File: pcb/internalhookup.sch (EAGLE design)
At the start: 10 parts, among them CN1 LASER, J1 CONTROL, J2 SERVO, J3 AZ_SENSOR, Q1 SMMBT2222ALT, Q2 SMMBT2222ALT, U1 AMS1117-3.3

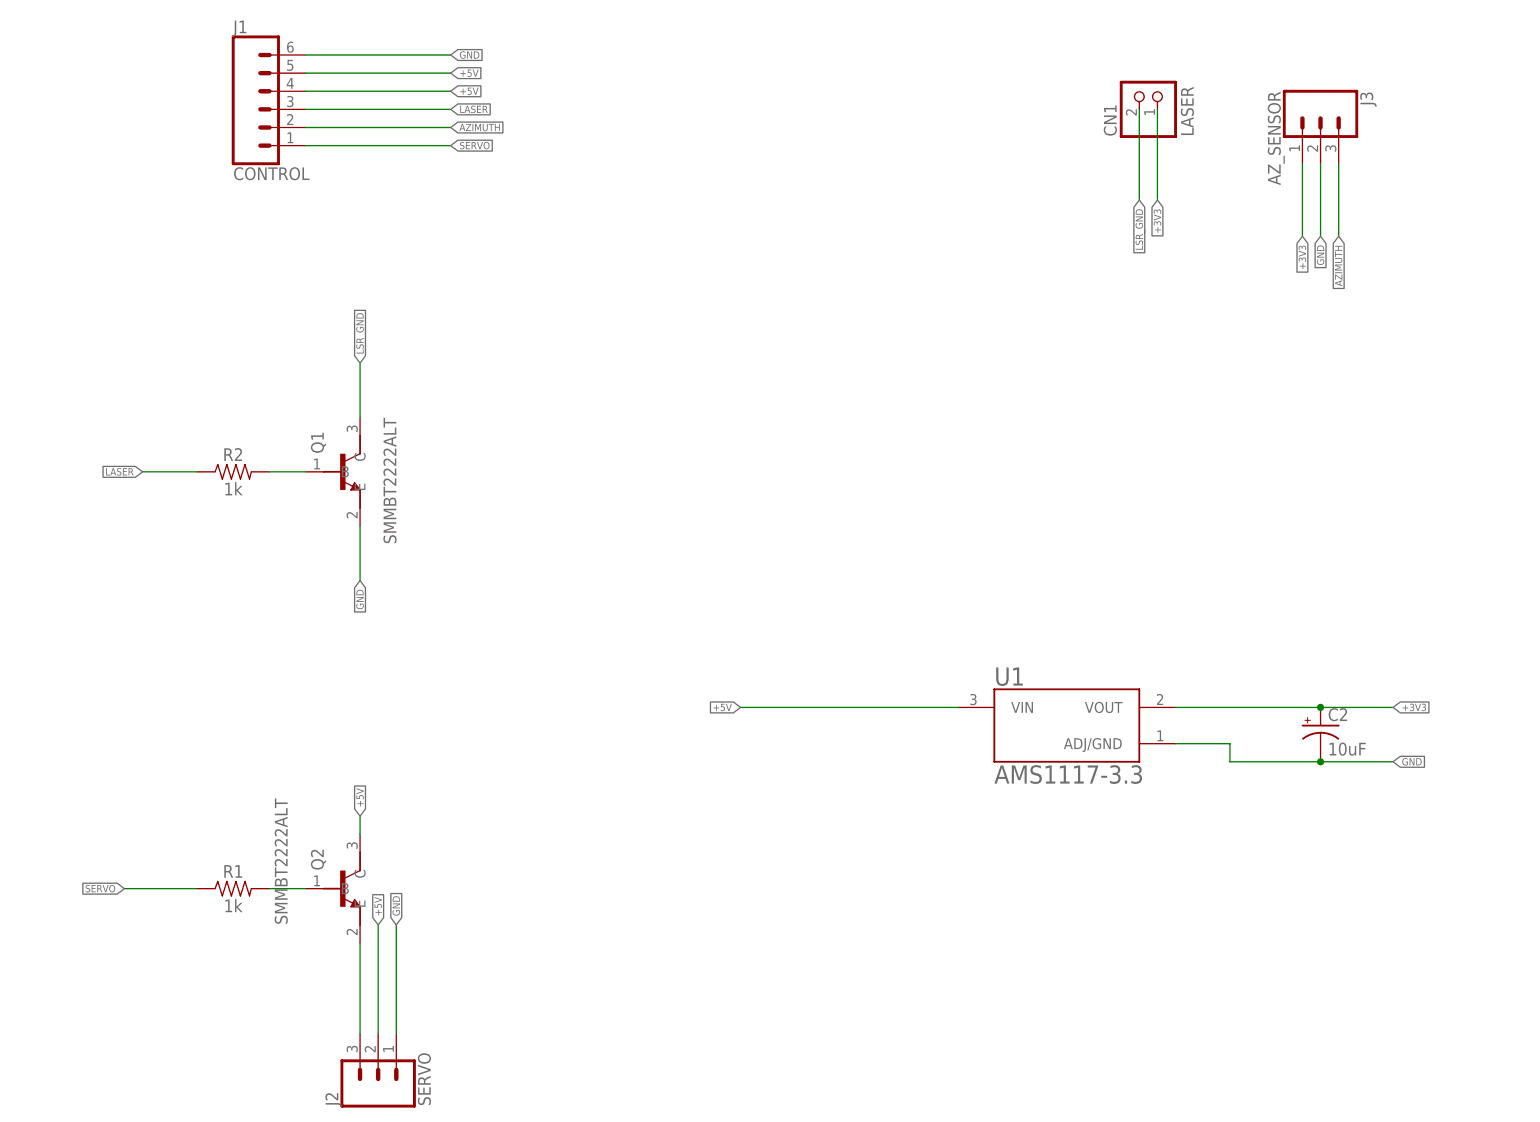
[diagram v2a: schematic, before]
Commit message: Lots of changes
* Dropped LED's and LASER control
* Renamed DECLINATION to AZIMUTH
* Moved AZIMUTH control hookup into the globe (it needs to spin freely)

I couldn't make the LED's fit and shine without casting shadows inside
the globe. Plus, there wasn't much room, and it required more wires to
make work. No a critical problem, but the challenges outweighed the
benefits. I'm going to water color paint the globe now.

I also removed the LASER control, the manufacturer said don't duty cycle
it, the built in controls take care of it. This isn't supposed to be on
constantly anyway.
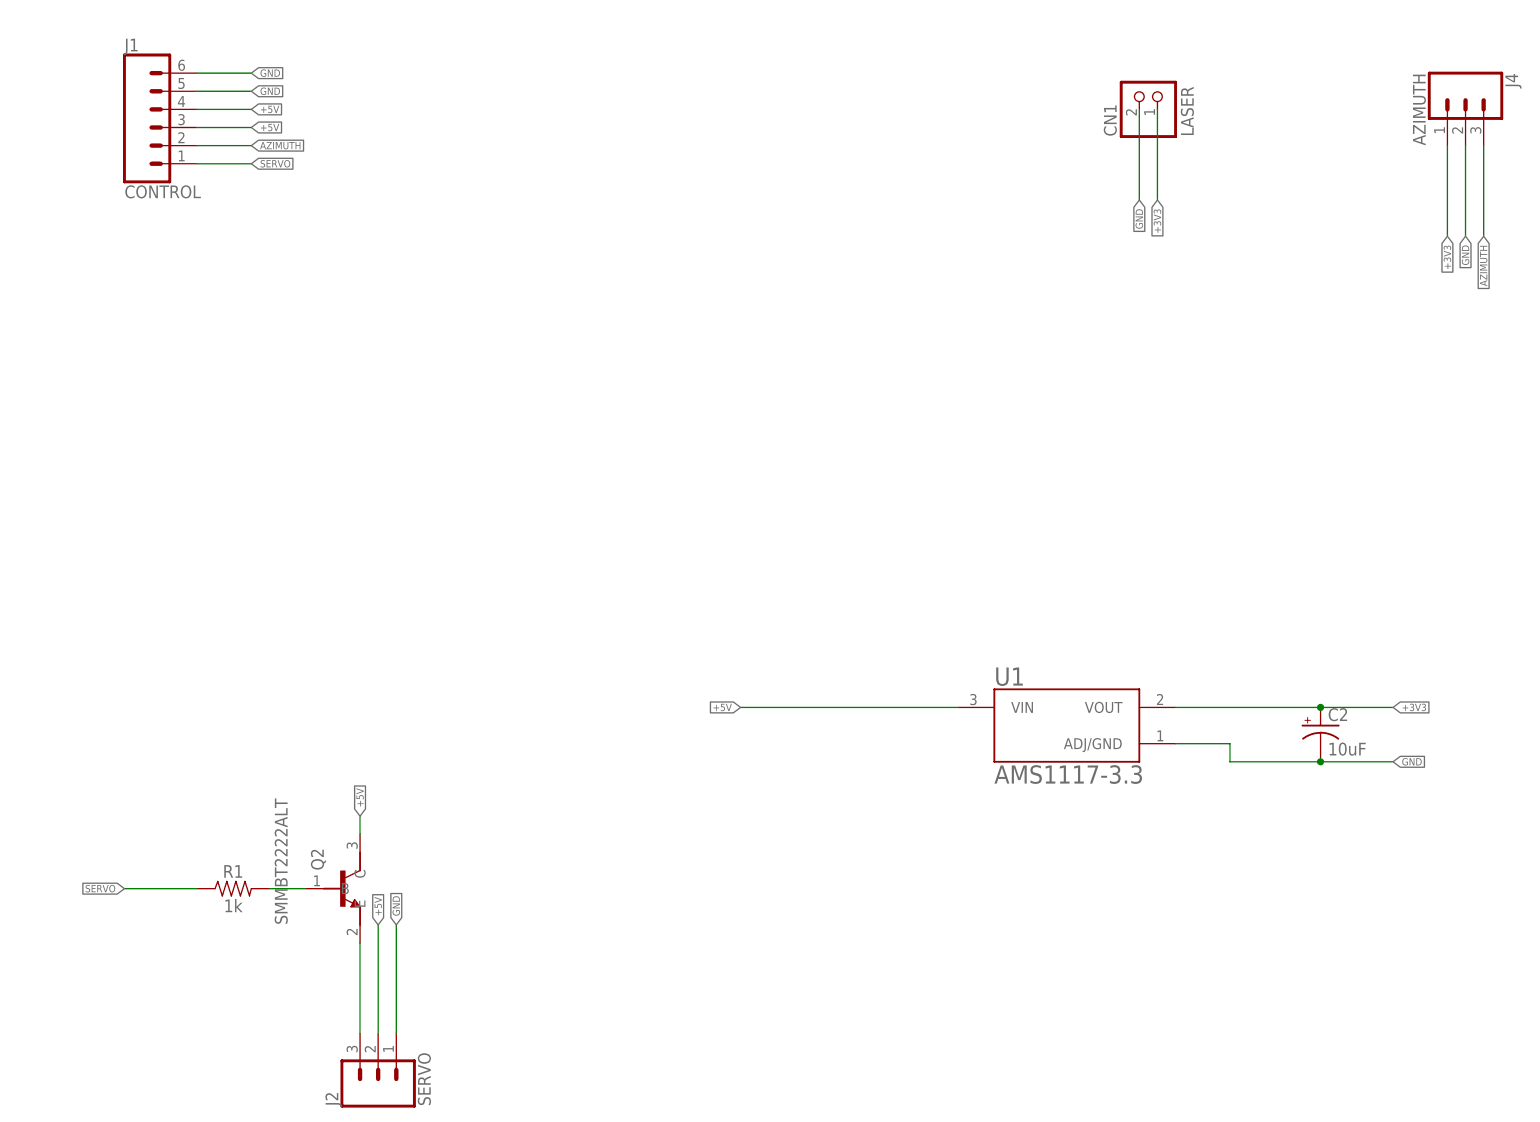
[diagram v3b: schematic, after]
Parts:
- removed J3: AZ_SENSOR, SparkFun-Connectors:CONN_03
- removed Q1: SMMBT2222ALT, MMBT3904:MMBT3904
- removed R2: 1k, SparkFun-Resistors:0.3OHM-0805-1/8W-1%
- added J4: AZIMUTH, SparkFun-Connectors:CONN_03
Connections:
- removed net LASER: J1.3, R2.1
- removed net LSR_GND: CN1.1, Q1.C
- removed net N$3: Q1.B, R2.2
- net +3V3: now also J4.1; no longer J3.1
- net +5V: now also J1.3; no longer J1.5
- net AZIMUTH: now also J4.3; no longer J3.3
- net GND: now also CN1.1, J1.5, J4.2; no longer J3.2, Q1.E
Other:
- moved on the sheet: J1
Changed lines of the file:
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@@
 <part name="CN1" library="adafruit" library_urn="urn:adsk.eagle:library:420" deviceset="JST_2PIN" device="-THM-RA" package3d_urn="urn:adsk.eagle:package:6240694/1" value=" LASER"/>
 <part name="U1" library="AMS1117-3.3" deviceset="AMS1117-3.3" device=""/>
+<part name="C2" library="SparkFun-Capacitors" library_urn="urn:adsk.eagle:library:510" deviceset="10UF-POLAR" device="-RADIAL-2.5MM-25V-20%" package3d_urn="urn:adsk.eagle:package:37423/1" value="10uF"/>
+<part name="Q2" library="MMBT3904" deviceset="MMBT3904" device="" value="SMMBT2222ALT"/>
 <part name="J1" library="SparkFun-Connectors" library_urn="urn:adsk.eagle:library:513" deviceset="CONN_06" device="SILK_FEMALE_PTH" package3d_urn="urn:adsk.eagle:package:38009/1" value="CONTROL"/>
-<part name="C2" library="SparkFun-Capacitors" library_urn="urn:adsk.eagle:library:510" deviceset="10UF-POLAR" device="-RADIAL-2.5MM-25V-20%" package3d_urn="urn:adsk.eagle:package:37423/1" value="10uF"/>
-<part name="J3" library="SparkFun-Connectors" library_urn="urn:adsk.eagle:library:513" deviceset="CONN_03" device="" package3d_urn="urn:adsk.eagle:package:38063/1" value="AZ_SENSOR"/>
-<part name="Q2" library="MMBT3904" deviceset="MMBT3904" device="" value="SMMBT2222ALT"/>
-<part name="Q1" library="MMBT3904" deviceset="MMBT3904" device="" value="SMMBT2222ALT"/>
-<part name="R2" library="SparkFun-Resistors" library_urn="urn:adsk.eagle:library:532" deviceset="0.3OHM" device="-0805-1/8W-1%" package3d_urn="urn:adsk.eagle:package:39651/1" value="1k"/>
+<part name="J4" library="SparkFun-Connectors" library_urn="urn:adsk.eagle:library:513" deviceset="CONN_03" device="" package3d_urn="urn:adsk.eagle:package:38063/1" value="AZIMUTH"/>
 </parts>
 <sheets>
@@
 <attribute name="VALUE" x="152.3908" y="85.844640625" size="2.5423" layer="96"/>
 </instance>
-<instance part="J1" gate="G$1" x="50.8" y="180.34" smashed="yes">
-<attribute name="VALUE" x="45.72" y="170.434" size="1.778" layer="96" font="vector"/>
-<attribute name="NAME" x="45.72" y="191.008" size="1.778" layer="95" font="vector"/>
-</instance>
 <instance part="C2" gate="G$1" x="198.12" y="93.98" smashed="yes">
 <attribute name="NAME" x="199.136" y="94.615" size="1.778" layer="95" font="vector"/>
 <attribute name="VALUE" x="199.136" y="89.789" size="1.778" layer="96" font="vector"/>
-</instance>
-<instance part="J3" gate="J$1" x="198.12" y="180.34" smashed="yes" rot="R270">
-<attribute name="VALUE" x="190.754" y="182.88" size="1.778" layer="96" font="vector" rot="R270"/>
-<attribute name="NAME" x="203.708" y="182.88" size="1.778" layer="95" font="vector" rot="R270"/>
 </instance>
 <instance part="Q2" gate="G$1" x="60.96" y="71.12" smashed="yes">
@@
 <attribute name="VALUE" x="53.34501875" y="66.050040625" size="1.781509375" layer="96" rot="R90"/>
 </instance>
-<instance part="Q1" gate="G$1" x="60.96" y="129.54" smashed="yes">
-<attribute name="NAME" x="58.42" y="132.083840625" size="1.779340625" layer="95" rot="R90"/>
-<attribute name="VALUE" x="68.58501875" y="119.390040625" size="1.781509375" layer="96" rot="R90"/>
+<instance part="J1" gate="G$1" x="35.56" y="177.8" smashed="yes">
+<attribute name="VALUE" x="30.48" y="167.894" size="1.778" layer="96" font="vector"/>
+<attribute name="NAME" x="30.48" y="188.468" size="1.778" layer="95" font="vector"/>
 </instance>
-<instance part="R2" gate="G$1" x="45.72" y="129.54" smashed="yes">
-<attribute name="NAME" x="45.72" y="131.064" size="1.778" layer="95" font="vector" align="bottom-center"/>
-<attribute name="VALUE" x="45.72" y="128.016" size="1.778" layer="96" font="vector" align="top-center"/>
+<instance part="J4" gate="J$1" x="218.44" y="182.88" smashed="yes" rot="R270">
+<attribute name="VALUE" x="211.074" y="185.42" size="1.778" layer="96" font="vector" rot="R270"/>
+<attribute name="NAME" x="224.028" y="185.42" size="1.778" layer="95" font="vector" rot="R270"/>
 </instance>
 </instances>
@@
 </segment>
 <segment>
-<wire x1="55.88" y1="187.96" x2="76.2" y2="187.96" width="0.1524" layer="91"/>
-<label x="76.2" y="187.96" size="1.016" layer="95" xref="yes"/>
+<wire x1="40.64" y1="185.42" x2="48.26" y2="185.42" width="0.1524" layer="91"/>
+<label x="48.26" y="185.42" size="1.016" layer="95" xref="yes"/>
 <pinref part="J1" gate="G$1" pin="6"/>
 </segment>
 <segment>
-<pinref part="J3" gate="J$1" pin="2"/>
-<wire x1="198.12" y1="172.72" x2="198.12" y2="162.56" width="0.1524" layer="91"/>
-<label x="198.12" y="162.56" size="1.016" layer="95" rot="R270" xref="yes"/>
+<pinref part="CN1" gate="G$1" pin="1"/>
+<wire x1="172.72" y1="180.34" x2="172.72" y2="167.64" width="0.1524" layer="91"/>
+<label x="172.72" y="167.64" size="1.016" layer="95" rot="R270" xref="yes"/>
 </segment>
 <segment>
-<pinref part="Q1" gate="G$1" pin="E"/>
-<wire x1="63.5" y1="121.92" x2="63.5" y2="114.3" width="0.1524" layer="91"/>
-<label x="63.5" y="114.3" size="1.016" layer="95" rot="R270" xref="yes"/>
+<pinref part="J4" gate="J$1" pin="2"/>
+<wire x1="218.44" y1="175.26" x2="218.44" y2="162.56" width="0.1524" layer="91"/>
+<label x="218.44" y="162.56" size="1.016" layer="95" rot="R270" xref="yes"/>
+</segment>
+<segment>
+<wire x1="40.64" y1="182.88" x2="48.26" y2="182.88" width="0.1524" layer="91"/>
+<label x="48.26" y="182.88" size="1.016" layer="95" xref="yes"/>
+<pinref part="J1" gate="G$1" pin="5"/>
 </segment>
 </net>
@@
 </segment>
 <segment>
-<wire x1="55.88" y1="182.88" x2="76.2" y2="182.88" width="0.1524" layer="91"/>
-<label x="76.2" y="182.88" size="1.016" layer="95" xref="yes"/>
 <pinref part="J1" gate="G$1" pin="4"/>
+<wire x1="40.64" y1="180.34" x2="48.26" y2="180.34" width="0.1524" layer="91"/>
+<label x="48.26" y="180.34" size="1.016" layer="95" xref="yes"/>
 </segment>
 <segment>
-<wire x1="55.88" y1="185.42" x2="76.2" y2="185.42" width="0.1524" layer="91"/>
-<label x="76.2" y="185.42" size="1.016" layer="95" xref="yes"/>
-<pinref part="J1" gate="G$1" pin="5"/>
+<wire x1="40.64" y1="177.8" x2="48.26" y2="177.8" width="0.1524" layer="91"/>
+<label x="48.26" y="177.8" size="1.016" layer="95" xref="yes"/>
+<pinref part="J1" gate="G$1" pin="3"/>
 </segment>
 </net>
@@
 </segment>
 <segment>
-<pinref part="J3" gate="J$1" pin="1"/>
-<wire x1="195.58" y1="172.72" x2="195.58" y2="162.56" width="0.1524" layer="91"/>
-<label x="195.58" y="162.56" size="1.016" layer="95" rot="R270" xref="yes"/>
+<pinref part="J4" gate="J$1" pin="1"/>
+<wire x1="215.9" y1="175.26" x2="215.9" y2="162.56" width="0.1524" layer="91"/>
+<label x="215.9" y="162.56" size="1.016" layer="95" rot="R270" xref="yes"/>
 </segment>
 </net>
@@
 </segment>
 <segment>
-<wire x1="55.88" y1="175.26" x2="76.2" y2="175.26" width="0.1524" layer="91"/>
-<label x="76.2" y="175.26" size="1.016" layer="95" xref="yes"/>
 <pinref part="J1" gate="G$1" pin="1"/>
+<wire x1="40.64" y1="172.72" x2="48.26" y2="172.72" width="0.1524" layer="91"/>
+<label x="48.26" y="172.72" size="1.016" layer="95" xref="yes"/>
 </segment>
 </net>
@@
 <net name="AZIMUTH" class="0">
 <segment>
-<wire x1="55.88" y1="177.8" x2="76.2" y2="177.8" width="0.1524" layer="91"/>
-<label x="76.2" y="177.8" size="1.016" layer="95" xref="yes"/>
-<pinref part="J1" gate="G$1" pin="2"/>
+<pinref part="J4" gate="J$1" pin="3"/>
+<wire x1="220.98" y1="175.26" x2="220.98" y2="162.56" width="0.1524" layer="91"/>
+<label x="220.98" y="162.56" size="1.016" layer="95" rot="R270" xref="yes"/>
 </segment>
 <segment>
-<pinref part="J3" gate="J$1" pin="3"/>
-<wire x1="200.66" y1="172.72" x2="200.66" y2="162.56" width="0.1524" layer="91"/>
-<label x="200.66" y="162.56" size="1.016" layer="95" rot="R270" xref="yes"/>
+<pinref part="J1" gate="G$1" pin="2"/>
+<wire x1="40.64" y1="175.26" x2="48.26" y2="175.26" width="0.1524" layer="91"/>
+<label x="48.26" y="175.26" size="1.016" layer="95" xref="yes"/>
 </segment>
 </net>
-<net name="LASER" class="0">
-<segment>
-<wire x1="55.88" y1="180.34" x2="76.2" y2="180.34" width="0.1524" layer="91"/>
-<label x="76.2" y="180.34" size="1.016" layer="95" xref="yes"/>
-<pinref part="J1" gate="G$1" pin="3"/>
-</segment>
-<segment>
-<pinref part="R2" gate="G$1" pin="1"/>
-<wire x1="40.64" y1="129.54" x2="33.02" y2="129.54" width="0.1524" layer="91"/>
-<label x="33.02" y="129.54" size="1.016" layer="95" rot="R180" xref="yes"/>
-</segment>
-</net>
-<net name="N$3" class="0">
-<segment>
-<pinref part="Q1" gate="G$1" pin="B"/>
-<pinref part="R2" gate="G$1" pin="2"/>
-<wire x1="55.88" y1="129.54" x2="50.8" y2="129.54" width="0.1524" layer="91"/>
-</segment>
-</net>
-<net name="LSR_GND" class="0">
-<segment>
-<pinref part="Q1" gate="G$1" pin="C"/>
-<wire x1="63.5" y1="137.16" x2="63.5" y2="144.78" width="0.1524" layer="91"/>
-<label x="63.5" y="144.78" size="1.016" layer="95" rot="R90" xref="yes"/>
-</segment>
-<segment>
-<wire x1="172.72" y1="180.34" x2="172.72" y2="167.64" width="0.1524" layer="91"/>
-<label x="172.72" y="167.64" size="1.016" layer="95" rot="R270" xref="yes"/>
-<pinref part="CN1" gate="G$1" pin="1"/>
-</segment>
-</net>
